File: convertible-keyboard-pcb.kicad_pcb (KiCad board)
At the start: 2 copper layers, 2.2 x 1.9 mm, 486 parts, among them J1 USB_C, J2 Pico-EZmate 78171-0004, J3 JST-SH SM04B-SRSS-TB, Q1 AO3400A, Q2 2N7002, Q3 2N7002, SW1 SW_Push, SW10 SW_Push, SW100 SW_Push, SW101 SW_Push, SW102 SW_Push, SW103 SW_Push, SW104 SW_Push, SW105 SW_Push, SW106 SW_Push, SW107 SW_Push, SW108 SW_Push, SW11 SW_Push, SW12 SW_Push, SW13 SW_Push, SW14 SW_Push, SW15 SW_Push, SW16 SW_Push, SW17 SW_Push, SW18 SW_Push, SW19 SW_Push, SW2 SW_Push, SW20 SW_Push, SW201 SW_Push, SW202 SW_Push, SW21 SW_Push, SW22 SW_Push, SW23 SW_Push, SW24 SW_Push, SW25 SW_Push, SW26 SW_Push, SW27 SW_Push, SW28 SW_Push, SW29 SW_Push, SW3 SW_Push, SW30 SW_Push, SW31 SW_Push, SW32 SW_Push, SW33 SW_Push, SW34 SW_Push, SW35 SW_Push, SW36 SW_Push, SW37 SW_Push, SW38 SW_Push, SW39 SW_Push, SW4 SW_Push, SW40 SW_Push, SW41 SW_Push, SW42 SW_Push, SW43 SW_Push, SW44 SW_Push, SW45 SW_Push, SW46 SW_Push, SW47 SW_Push, SW48 SW_Push, SW49 SW_Push, SW5 SW_Push, SW50 SW_Push, SW51 SW_Push, SW52 SW_Push, SW53 SW_Push, SW54 SW_Push, SW55 SW_Push, SW56 SW_Push, SW57 SW_Push, SW58 SW_Push, SW59 SW_Push, SW6 SW_Push, SW60 SW_Push, SW61 SW_Push, SW62 SW_Push, SW63 SW_Push, SW64 SW_Push, SW65 SW_Push, SW66 SW_Push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

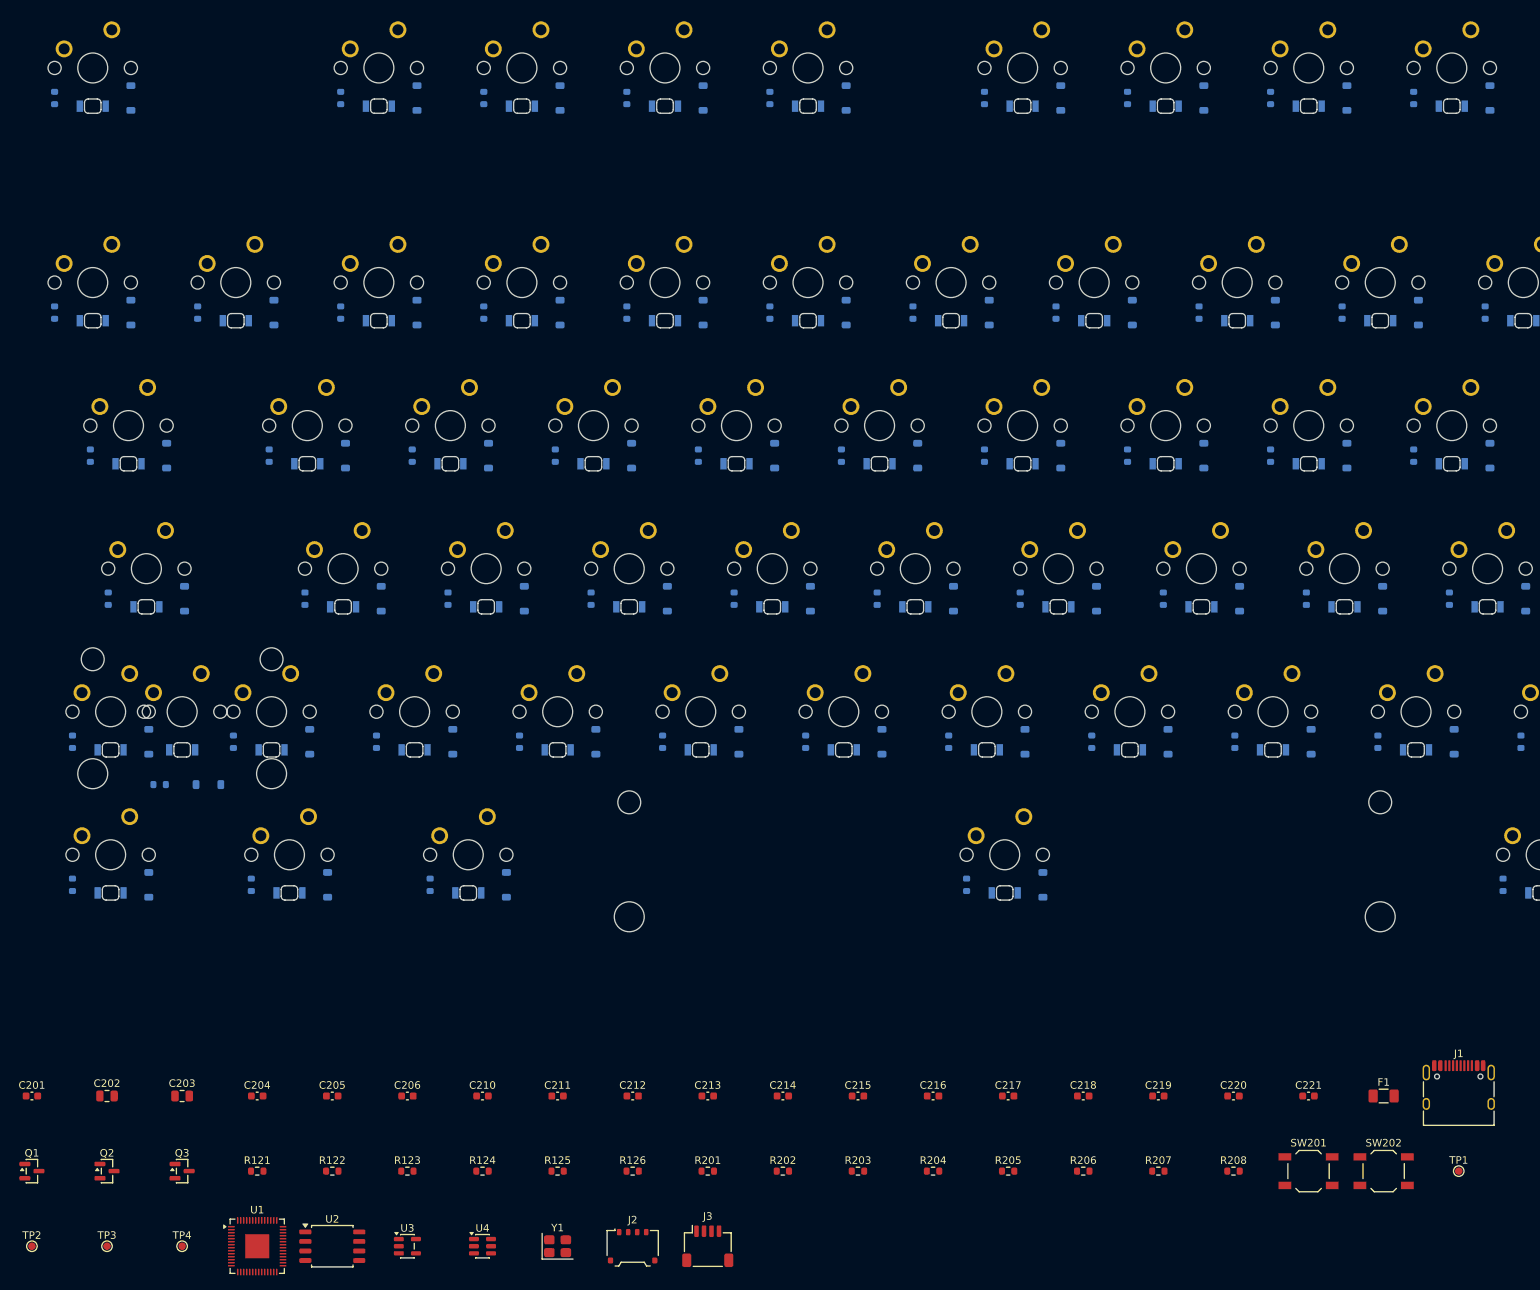
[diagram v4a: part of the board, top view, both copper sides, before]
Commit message: Vorläufige Platzierung von Controller, USB und Treibern
Alles auf der Rückseite in Flächen, die zwischen Schalterpins, Dioden,
Vorwiderständen und LED-Aussparungen frei sind:

- Esc/F1-Lücke: USB-C J1 an der Oberkante (Kontakte nach innen), darunter
  ESD-Schutz, CC- und Schirmbeschaltung, 27-Ohm-Widerstände, Polyfuse,
  3,3-V-Regler, Daughterboard-Stecker J2 (Pico-EZmate) und J3 (JST-SH)
- Streifen unter der F-Reihe: Flash, RP2040 (USB/QSPI-Seite nach links,
  Quarz rechts), Entkopplung in Reihen über und unter dem Chip, Quarz,
  BOOTSEL- und RESET-Taster, SWD-Testpads
- F4/F5-Lücke: Treiber Q1–Q3 mit Gate- und Pulldown-Widerständen
- Referenztexte der dicht gesetzten Entkopplungskondensatoren und
  Testpads auf dem Silkscreen ausgeblendet

DRC ohne Fehler, keine Courtyard-Überlappungen, Parität sauber.
Feinschliff der Lage erfolgt beim Routing.

Co-Authored-By: Claude Opus 5 (1M context) <noreply@anthropic.com>
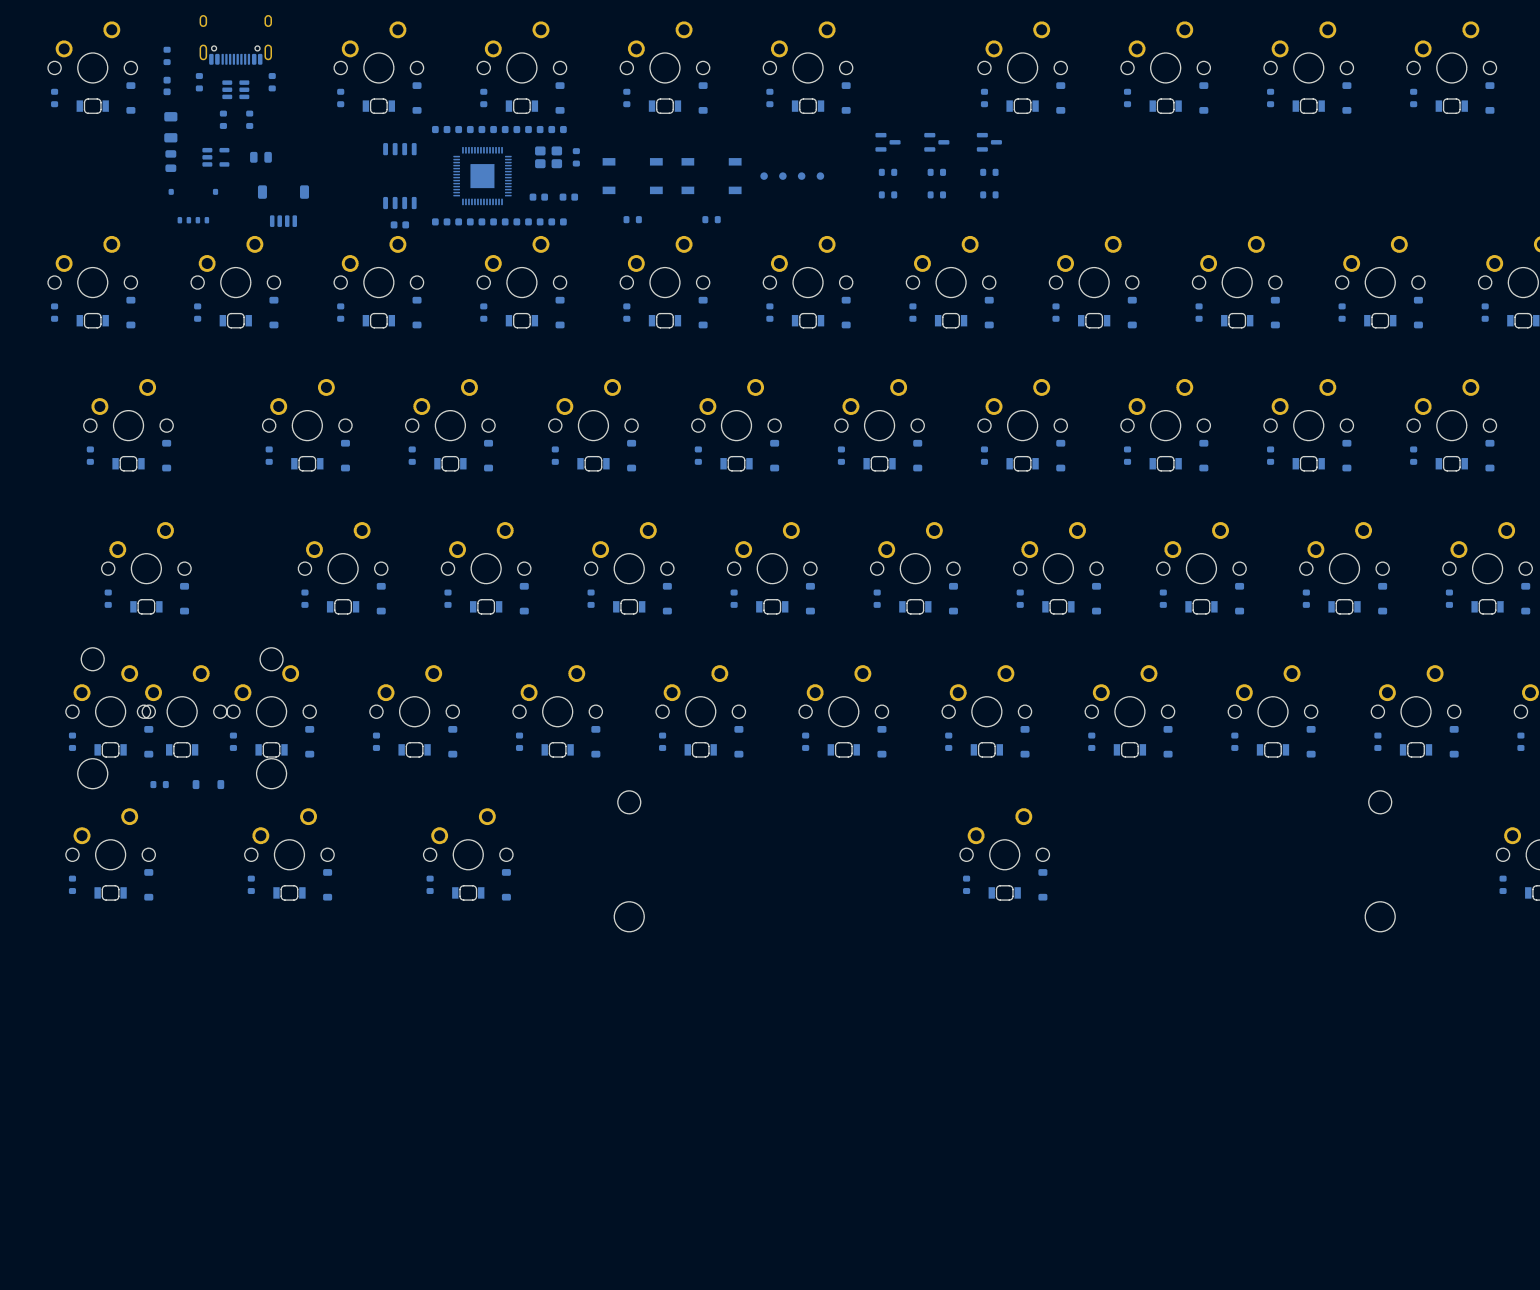
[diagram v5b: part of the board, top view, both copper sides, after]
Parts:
- C201, C202, C203, C204, C205, C206, C210, C211, C212, C213, C214, C215, C216, C217, C218, C219, C220, C221, F1, J1, J2, J3, Q1, Q2, Q3, R121, R122, R123, R124, R125, R126, R201, R202, R203, R204, R205, R206, R207, R208, SW201, SW202, TP1, TP2, TP3, TP4, U1, U2, U3, U4, Y1: moved to B.Cu
- moved J1 216.1 mm to (57.1, 32.9)
- moved F1 206.7 mm to (48.5, 46.0), turned to 90 degrees
- moved Q1 178.2 mm to (144.0, 48.0)
- moved Q2 176.0 mm to (150.5, 48.0)
- moved R203 174.7 mm to (48.0, 36.5), turned to 90 degrees
- moved Q3 174.1 mm to (157.5, 48.0)
- moved TP2 174.1 mm to (130.0, 52.5)
- moved R205 172.6 mm to (59.0, 45.0), turned to 90 degrees
- moved TP3 169.9 mm to (132.5, 52.5)
- moved R204 168.9 mm to (55.5, 45.0), turned to 90 degrees
- moved SW202 166.0 mm to (110.0, 52.5)
- moved TP4 165.9 mm to (135.0, 52.5)
- moved TP1 161.6 mm to (127.5, 52.5)
- moved R202 160.2 mm to (62.0, 40.0), turned to 90 degrees
- moved R201 160.0 mm to (52.3, 40.0), turned to 90 degrees
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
